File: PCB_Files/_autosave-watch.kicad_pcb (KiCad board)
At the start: 4 copper layers, 40 x 40 mm, 118 parts, among them J1 Conn_01x13_MountingPin, J3 Conn_01x02_Pin, P1 USB_C_Plug_USB2.0, Q1 BC847, Q2 BC847, Q3 FS8205A, Q4 BSS138, Q5 BSS138, Q8 BC847, SW1 SW_Push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

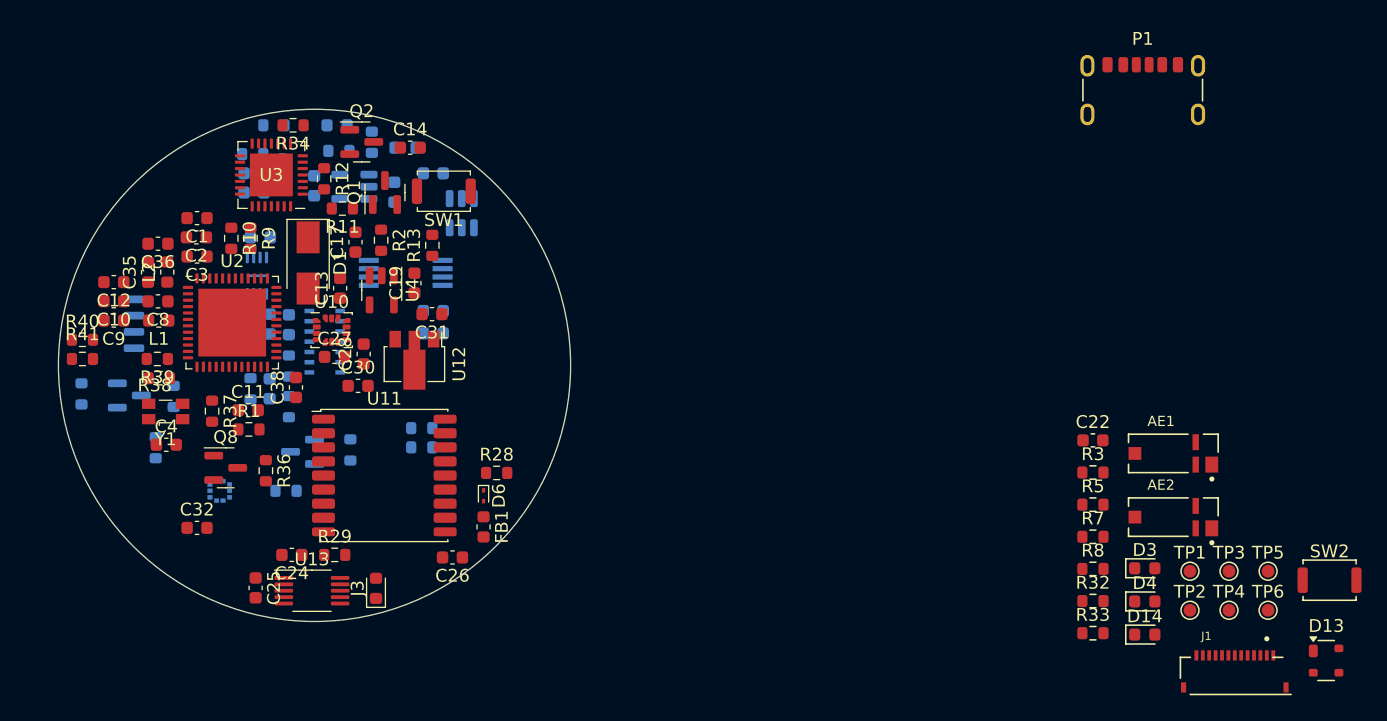
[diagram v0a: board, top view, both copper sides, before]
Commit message: Added new ZIF connector footprint and made changes in schematics
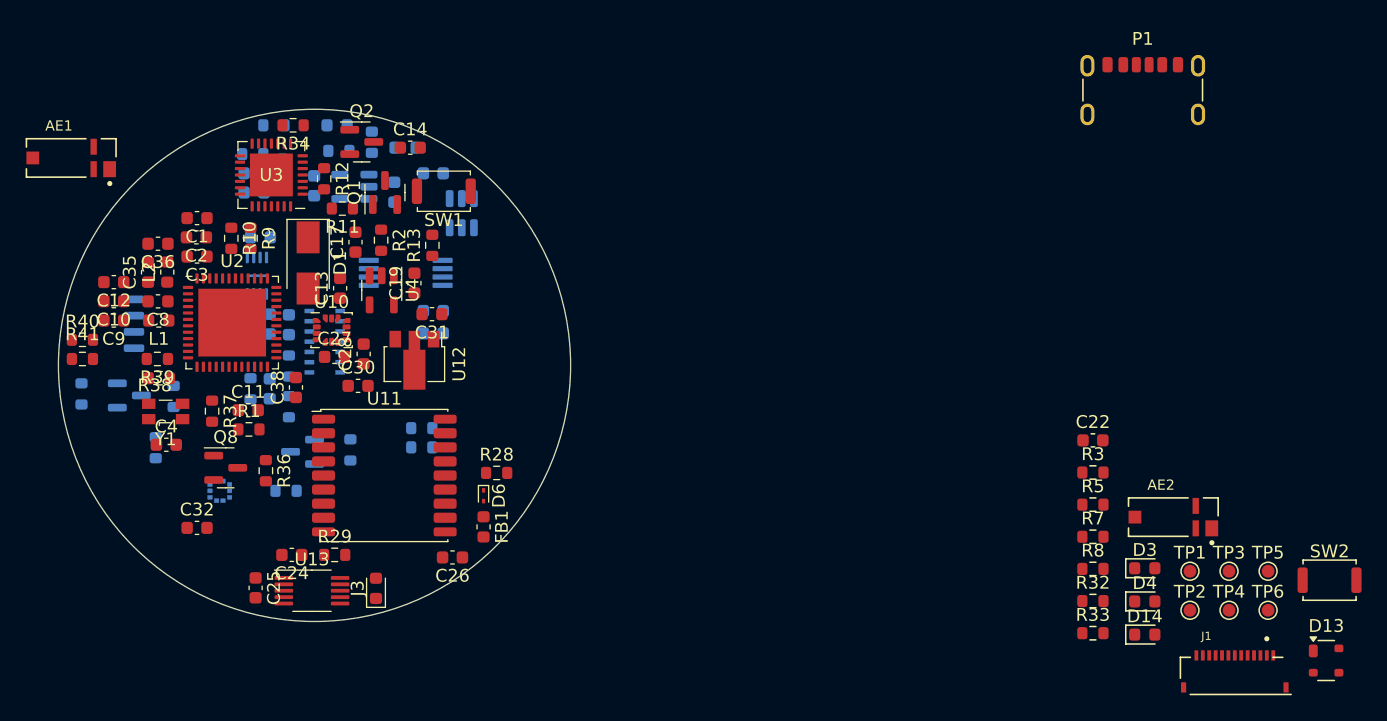
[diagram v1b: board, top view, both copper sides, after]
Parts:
- moved AE1 89.1 mm to (131.0, 83.8)
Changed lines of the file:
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@@
 	(footprint "footprints:XCVR_NN03-320"
 		(layer "F.Cu")
-		(at 217.07 106.875)
+		(at 131 83.8)
 		(property "Reference" "AE1"
 			(at -0.96 -2.508 0)
@@
 			(polygon
 				(pts
-					(xy 213.57 106.375) (xy 213.57 105.375) (xy 218.57 105.375) (xy 218.57 106.625) (xy 219.07 106.625)
-					(xy 219.07 105.375) (xy 220.57 105.375) (xy 220.57 107.125) (xy 219.57 107.125) (xy 219.57 108.375)
-					(xy 219.07 108.375) (xy 219.07 107.125) (xy 218.57 107.125) (xy 218.57 108.375) (xy 213.57 108.375)
-					(xy 213.57 107.375) (xy 214.57 107.375) (xy 214.57 106.375)
+					(xy 127.5 83.3) (xy 127.5 82.3) (xy 132.5 82.3) (xy 132.5 83.55) (xy 133 83.55) (xy 133 82.3) (xy 134.5 82.3)
+					(xy 134.5 84.05) (xy 133.5 84.05) (xy 133.5 85.3) (xy 133 85.3) (xy 133 84.05) (xy 132.5 84.05)
+					(xy 132.5 85.3) (xy 127.5 85.3) (xy 127.5 84.3) (xy 128.5 84.3) (xy 128.5 83.3)
 				)
 			)
@@
 			(polygon
 				(pts
-					(xy 213.57 106.375) (xy 213.57 105.375) (xy 218.57 105.375) (xy 218.57 106.625) (xy 219.07 106.625)
-					(xy 219.07 105.375) (xy 220.57 105.375) (xy 220.57 107.125) (xy 219.57 107.125) (xy 219.57 108.375)
-					(xy 219.07 108.375) (xy 219.07 107.125) (xy 218.57 107.125) (xy 218.57 108.375) (xy 213.57 108.375)
-					(xy 213.57 107.375) (xy 214.57 107.375) (xy 214.57 106.375)
-				)
-			)
+					(xy 127.5 83.3) (xy 127.5 82.3) (xy 132.5 82.3) (xy 132.5 83.55) (xy 133 83.55) (xy 133 82.3) (xy 134.5 82.3)
+					(xy 134.5 84.05) (xy 133.5 84.05) (xy 133.5 85.3) (xy 133 85.3) (xy 133 84.05) (xy 132.5 84.05)
+					(xy 132.5 85.3) (xy 127.5 85.3) (xy 127.5 84.3) (xy 128.5 84.3) (xy 128.5 83.3)
+				)
+			)
